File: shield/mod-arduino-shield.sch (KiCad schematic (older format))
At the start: 48 parts, among them J1 RJHSE-5084, J2 RJHSE-5084, Q1 MMBT3904, U1 SN75176BDR

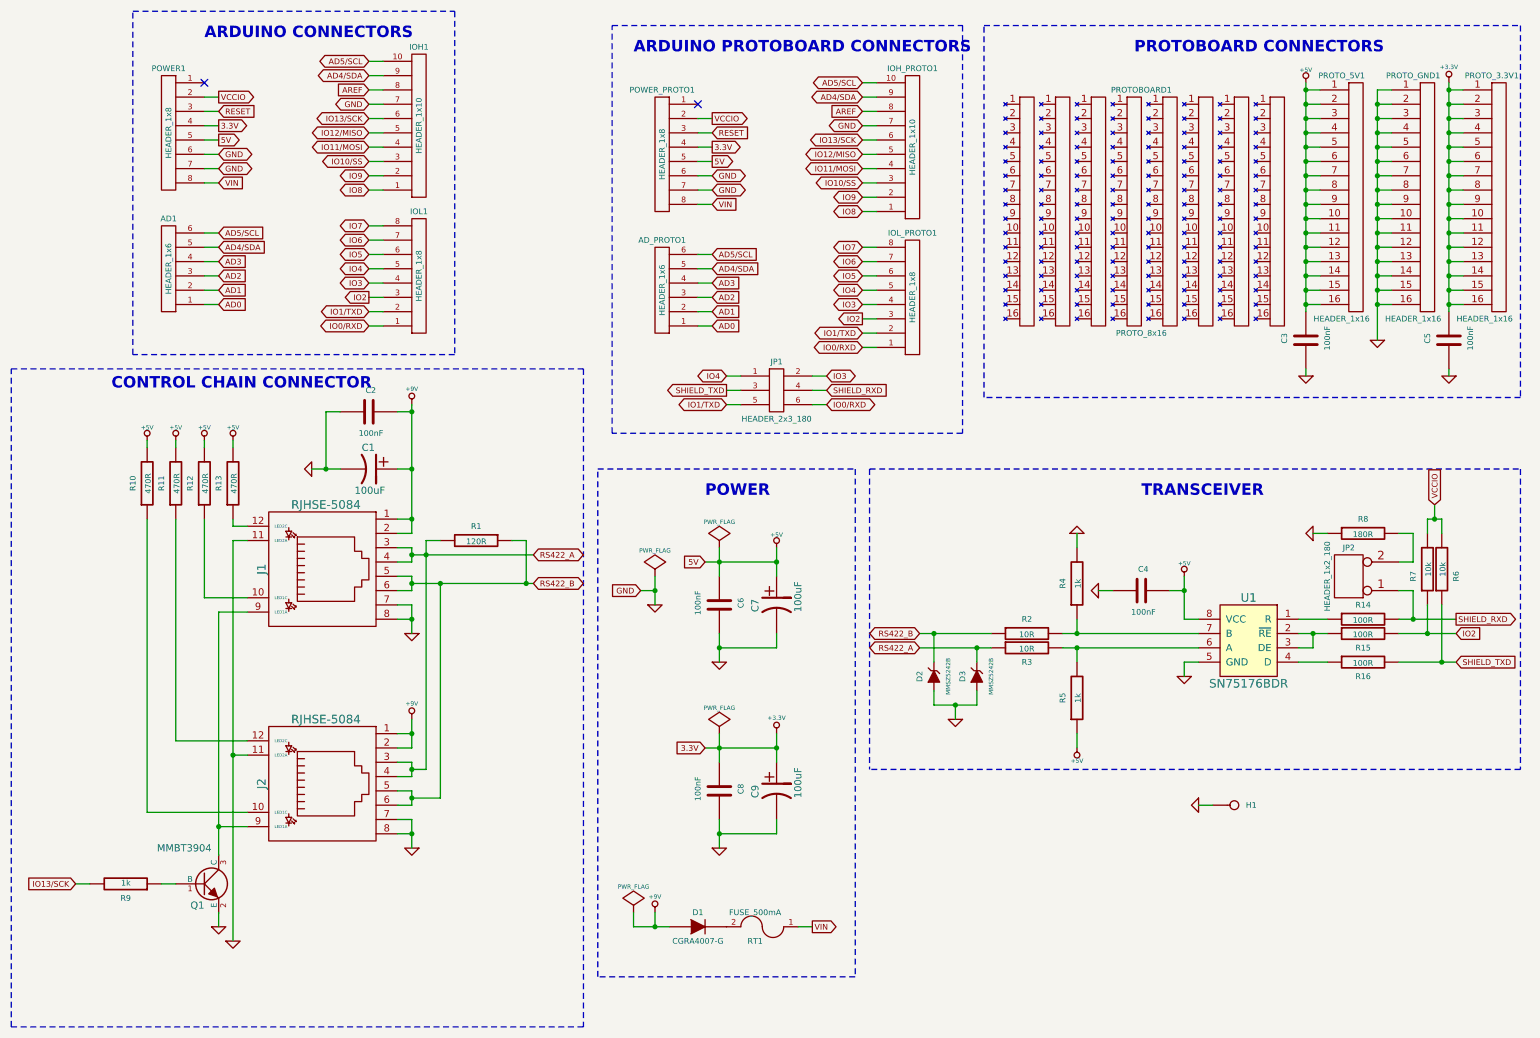
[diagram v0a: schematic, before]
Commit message: fix issue #2: rename VCCIO to IOREF
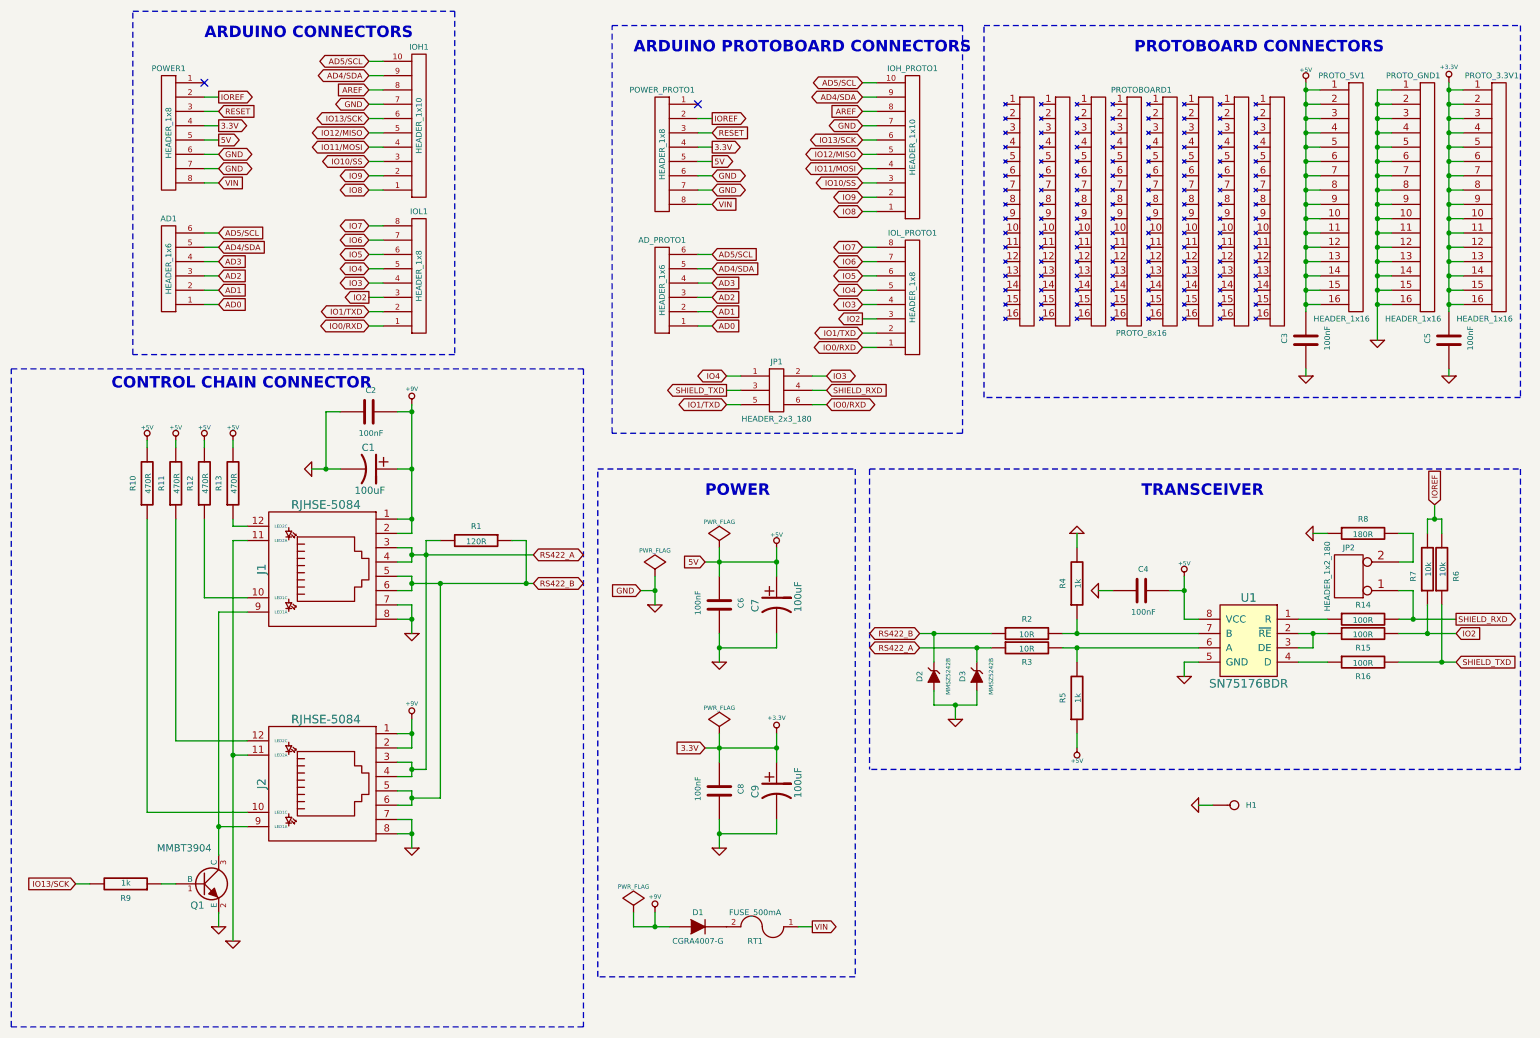
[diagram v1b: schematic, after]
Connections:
- net VCCIO renamed IOREF
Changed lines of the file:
@@
 	11100 5900 6550 5900
 Text GLabel 2000 1200 2    40   Output ~ 0
-VCCIO
+IOREF
 Wire Wire Line
 	1900 1200 2000 1200
 Text GLabel 5450 1350 2    40   Output ~ 0
-VCCIO
+IOREF
 Wire Wire Line
 	5350 1350 5450 1350
@@
 	10500 4150 10500 4050
 Text GLabel 10500 4050 1    40   Input ~ 0
-VCCIO
+IOREF
 $EndSCHEMATC

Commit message: fix issue #1: IOREF should not be used to power the circuit
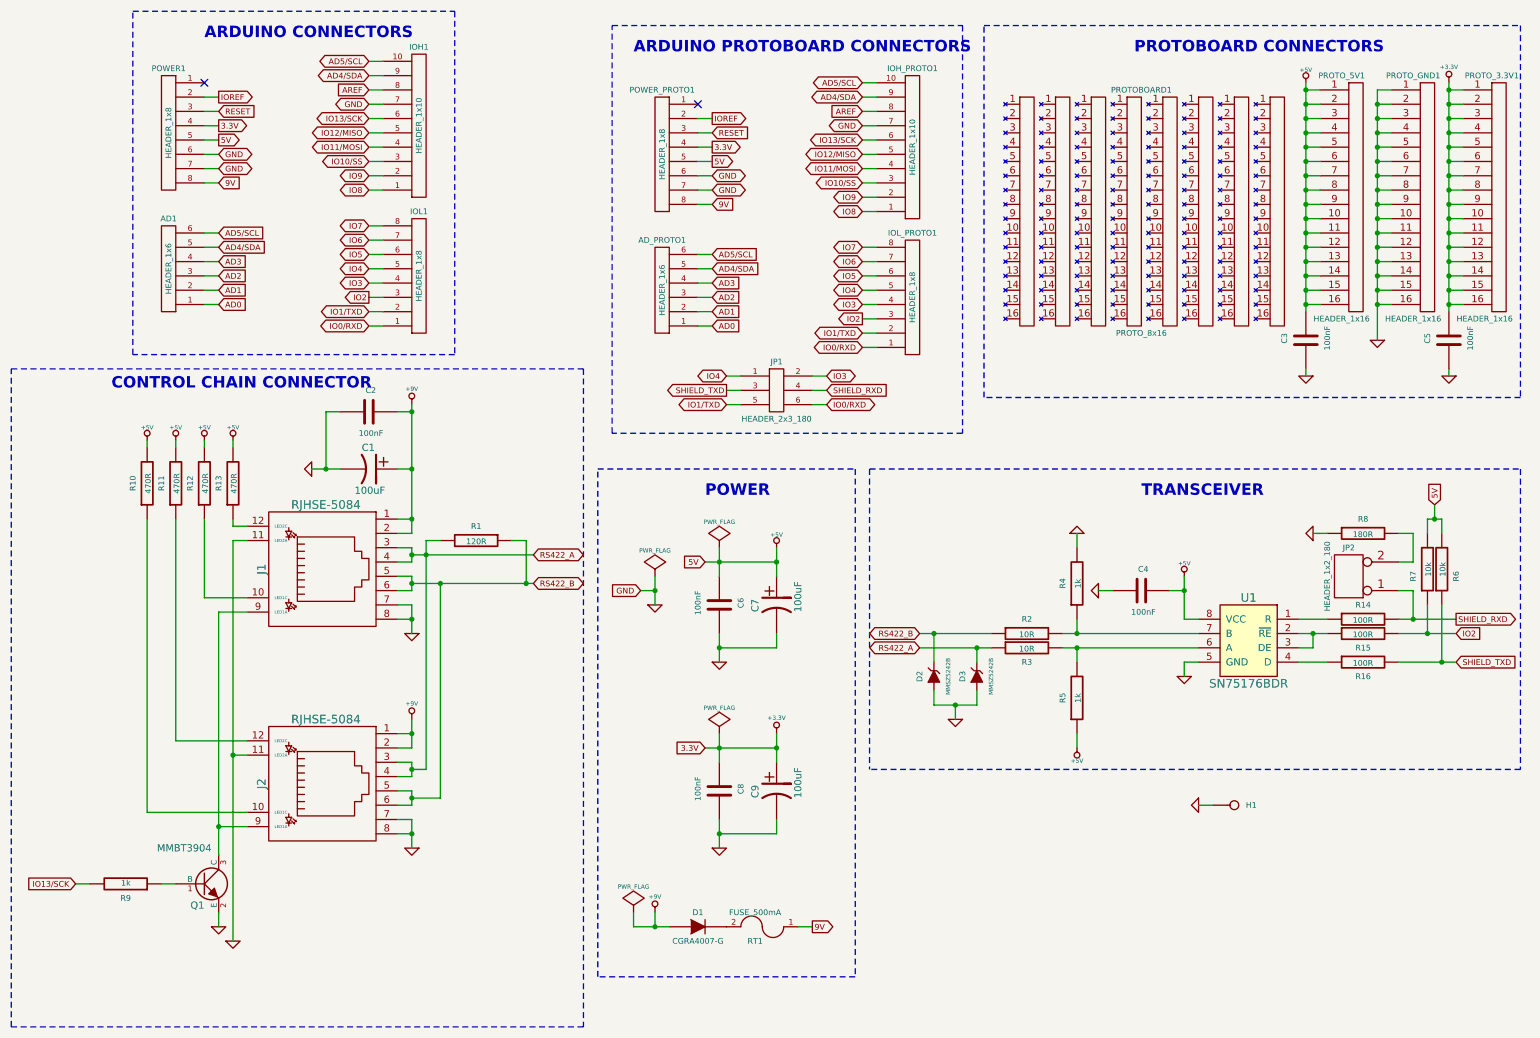
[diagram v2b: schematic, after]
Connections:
- net +5V: now also R6.2, R7.2
- net IOREF: no longer R6.2, R7.2
- net VIN renamed 9V
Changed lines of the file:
@@
 AD5/SCL
 Text GLabel 2000 1800 2    40   Input ~ 0
-VIN
+9V
 $Comp
 L +9V #PWR018
@@
 IO0/RXD
 Text GLabel 5450 1950 2    40   Input ~ 0
-VIN
+9V
 Text GLabel 6150 7000 2    40   Output ~ 0
-VIN
+9V
 $Comp
 L GND #PWR022
@@
 	10500 4150 10500 4050
 Text GLabel 10500 4050 1    40   Input ~ 0
-IOREF
+5V
 $EndSCHEMATC
